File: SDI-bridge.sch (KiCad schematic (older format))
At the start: 24 parts

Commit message: Add todos
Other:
- note added: "TODO: Add logotypes, use Antmicro and OSHW"
- note added: "TODO: Add partitioning to schematics and names for functional blocks"
- note added: "TODO: clarify pin naming - SDI and SDI with dash on top"
- note added: "TODO: make sure the components used there are 1%"
- note added: "TODO: multiple schematics are nice but maybe it would be good to place everything on a single sheet (say A2 format) Still we can downscale it to A4 for printing on paper."
- note added: "TODO: place resistor ladders on OUT signals"
- note added: "TODO: place testpads on sync signals"
- note added: "TODO: please name particular nets in the bus/harness"
- note added: "Would be good to have an on-board LED indicator for LOCKED\nLOCKED should also be exposed on b2b connector"
- note added: "how about using 2 B2B connectors ?\ntreat audio signals with lowest priority"
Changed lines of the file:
@@
 EESchema Schematic File Version 4
 LIBS:SDI-bridge-cache
-EELAYER 26 0
+EELAYER 30 0
 EELAYER END
 $Descr A3 16535 11693
@@
 Wire Bus Line
 	3650 6850 3650 7750
+Text Notes 12250 6550 0    50   ~ 0
+TODO: make sure the components used there are 1%
+Text Notes 5950 4050 0    50   ~ 0
+TODO: clarify pin naming - SDI and SDI with dash on top
+Text Notes 4900 4050 1    50   ~ 0
+TODO: please name particular nets in the bus/harness
+Text Notes 1300 1550 0    50   ~ 0
+Would be good to have an on-board LED indicator for LOCKED\nLOCKED should also be exposed on b2b connector
+Text Notes 850  2050 0    50   ~ 0
+TODO: place testpads on sync signals
+Text Notes 4200 1750 0    50   ~ 0
+TODO: place resistor ladders on OUT signals
+Text Notes 1600 9050 0    50   ~ 0
+how about using 2 B2B connectors ?\ntreat audio signals with lowest priority
+Text Notes 2000 10050 0    50   ~ 0
+TODO: Add partitioning to schematics and names for functional blocks
+Text Notes 3000 11050 0    50   ~ 0
+TODO: multiple schematics are nice but maybe it would be good to place everything on a single sheet (say A2 format) Still we can downscale it to A4 for printing on paper.
+Text Notes 3050 10800 0    50   ~ 0
+TODO: Add logotypes, use Antmicro and OSHW
 $EndSCHEMATC

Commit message: Add updated schematic
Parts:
- added C1, C10, C11, C12, C13, C14, C19, C2, C20, C3, C31, C32, C4, C5, C6, C7, C8, C9, C?: C_10n_0402, antmicro-footprints:0402-cap, symbol antmicroCapacitors0402:C_10n_0402
- added C16: C_33u_0603, antmicro-footprints:0603, symbol antmicroCapacitorspol:C_33u_0603
- added C26, C27, C29, C30, C?: C_1u_0402, antmicro-footprints:0402-cap, symbol antmicroCapacitors0402:C_1u_0402
- added C? (x2): C_10u_0603, antmicro-footprints:0603-cap, symbol antmicroCapacitors0603:C_10u_0603
- added D?: LG_L29K-G2J1-24-Z, antmicro-footprints:LED_0603, symbol antmicroLEDIndicationDiscrete:LG_L29K-G2J1-24-Z
- added J?: 3220-10-0100-00, antmicro-footprints:PinHeader_2x5_P1.27mm_Drill.7mm, symbol antmicroRectangularConnectorsHeadersMalePins:3220-10-0100-00
- added R10, R11, R12, R13, R14, R15, R16, R17, R18, R19, R20, R21, R22, R23, R30, R31, R32, R4, R5, R6, R7, R8, R9: R_0R_0402, antmicro-footprints:0402-res, symbol antmicroResistors0402:R_0R_0402
- added R26: R_105R_0402, antmicro-footprints:0402-res, symbol antmicroResistors0402:R_105R_0402
- added R? (x2): R_120k_0402, antmicro-footprints:0402-res, symbol antmicroResistors0402:R_120k_0402
- added R?: R_100R_0402, antmicro-footprints:0402-res, symbol antmicroResistors0402:R_100R_0402
- added TP1, TP2, TP?: TP_SMD1MM, antmicro-footprints:Testpoint_smd_1mm, symbol antmicroTestPoints:TP_SMD1MM
- added U?: MAX8902B, antmicro-footprints:TDFN2x2, symbol antmicroPMICVoltageRegulatorsLinear:MAX8902B
- gave numbers to parts that had none: 22
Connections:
- net labels added: +3.3V, D0, D1, D10, D11, D12, D13, D14, D15, D16, D17, D18, D19, D2, D3, D4, D5, D6, D7, D8, D9, DOUT0, DOUT1, DOUT10, DOUT11, DOUT12, DOUT13, DOUT14, DOUT15, DOUT16, DOUT17, DOUT18, DOUT19, DOUT2, DOUT3, DOUT4, DOUT5, DOUT6, DOUT7, DOUT8, DOUT9, NC
- wire segments 206 -> 424
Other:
- note added: "Jtag"
- note added: "Power Filtering"
- note added: "Power decoupling"
- note removed: "TODO: Add logotypes, use Antmicro and OSHW"
- note removed: "TODO: make sure the components used there are 1%"
- note removed: "TODO: multiple schematics are nice but maybe it would be good to place everything on a single sheet (say A2 format) Still we can downscale it to A4 for printing on paper."
- note removed: "TODO: place resistor ladders on OUT signals"
- note removed: "TODO: place testpads on sync signals"
- note removed: "TODO: please name particular nets in the bus/harness"
- note removed: "Would be good to have an on-board LED indicator for LOCKED\nLOCKED should also be exposed on b2b connector"
- moved on the sheet: C15, C17, C18, C21, C22, C23, C24, C25, C28, J1, J2, R1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

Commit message: Arrange pcb components and add jumpers and logo
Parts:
- added JP1, JP2, JP3, JP4, JP5, JP6: SolderJumper_3_Open, Jumper:SolderJumper-3_P1.3mm_Open_Pad1.0x1.5mm, symbol Jumper:SolderJumper_3_Open
- added N1: antmicro_logo, antmicro-footprints:antmicro-logo_scaled_20mm, symbol antmicroMechanicalParts:antmicro_logo
- added R36, R37, R38, R39, R40, R41: R_0R_0402, antmicro-footprints:0402-res, symbol antmicroResistors0402:R_0R_0402
- gave numbers to parts that had none: 11
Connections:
- wire segments 424 -> 448
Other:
- note added: "Do we need SDO?"
- note added: "Low noise LDO\n"
- note added: "Power supply"
- note added: "Where to connect this signal?"
- note added: "treat audio signals with lowest priority"
- note removed: "Jtag"
- note removed: "We need to choose some of this signals( if needed more space we can change connector to bigger one)"
- note removed: "how about using 2 B2B connectors ?\ntreat audio signals with lowest priority"
- moved on the sheet: C1, C10, C11, C12, C13, C14, C15, C16, C17, C18, C19, C2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

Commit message: Initial routing -WIP
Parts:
- C16: footprint antmicro-footprints:0603 -> antmicro-footprints:0603-cap
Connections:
- net D0: now also R23.2; no longer R4.1
- net D1: now also R22.2; no longer R5.1
- net D10: now also R4.2; no longer R14.1
- net D11: now also R5.2; no longer R15.1
- net D12: now also R6.2; no longer R16.1
- net D13: now also R7.2; no longer R17.1
- net D14: now also R8.2; no longer R18.1
- net D15: now also R9.2; no longer R19.1
- net D16: now also R10.2; no longer R20.1
- net D17: now also R11.2; no longer R21.1
- net D18: now also R12.2; no longer R22.1
- net D19: now also R13.2; no longer R23.1
- net D2: now also R21.2; no longer R6.1
- net D3: now also R20.2; no longer R7.1
- net D4: now also R19.2; no longer R8.1
- net D5: now also R18.2; no longer R9.1
- net D6: now also R17.2; no longer R10.1
- net D7: now also R16.2; no longer R11.1
- net D8: now also R15.2; no longer R12.1
- net D9: now also R14.2; no longer R13.1
- net DOUT0: now also J1.40, R23.1; no longer J1.21, R4.2
- net DOUT1: now also J1.39, R22.1; no longer J1.22, R5.2
- net DOUT10: now also J1.30, R4.1; no longer J1.31, R14.2
- net DOUT11: now also J1.29, R5.1; no longer J1.32, R15.2
- net DOUT12: now also J1.28, R6.1; no longer J1.33, R16.2
- net DOUT13: now also J1.27, R7.1; no longer J1.34, R17.2
- net DOUT14: now also J1.26, R8.1; no longer J1.35, R18.2
- net DOUT15: now also J1.25, R9.1; no longer J1.36, R19.2
- net DOUT16: now also J1.24, R10.1; no longer J1.37, R20.2
- net DOUT17: now also J1.23, R11.1; no longer J1.38, R21.2
- net DOUT18: now also J1.22, R12.1; no longer J1.39, R22.2
- net DOUT19: now also J1.21, R13.1; no longer J1.40, R23.2
- net DOUT2: now also J1.38, R21.1; no longer J1.23, R6.2
- net DOUT3: now also J1.37, R20.1; no longer J1.24, R7.2
- net DOUT4: now also J1.36, R19.1; no longer J1.25, R8.2
- net DOUT5: now also J1.35, R18.1; no longer J1.26, R9.2
- net DOUT6: now also J1.34, R17.1; no longer J1.27, R10.2
- net DOUT7: now also J1.33, R16.1; no longer J1.28, R11.2
- net DOUT8: now also J1.32, R15.1; no longer J1.29, R12.2
- net DOUT9: now also J1.31, R14.1; no longer J1.30, R13.2
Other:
- moved on the sheet: R10, R11, R12, R13, R14, R15, R16, R17, R18, R19, R20, R21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

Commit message: Add routing - WIP
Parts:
- added R42: R_0R_0402, antmicro-footprints:0402-res, symbol antmicroResistors0402:R_0R_0402
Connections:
- net +3V3: now also R42.1; no longer C2.1, C33.1, C4.1, C6.1, C8.1, U1.A7 (IO_VDD), U1.D10 (IO_VDD), U1.G10 (IO_VDD), U1.K7 (IO_VDD)
- net GNDREF: now also C36.2
- new net +VSW: C2.1, C33.1, C4.1, C6.1, C8.1, R42.2, U1.A7 (IO_VDD), U1.D10 (IO_VDD), U1.G10 (IO_VDD), U1.K7 (IO_VDD)
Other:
- moved on the sheet: C36
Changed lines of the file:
@@
-$EndComp
-$Comp
-L antmicroCapacitors0603:C_10u_0603 C36
-U 1 1 5E2677C8
-P 10700 13000
-F 0 "C36" H 10815 13045 60  0000 L CNN
-F 1 "C_10u_0603" H 10700 12850 60  0001 C CNN
-F 2 "antmicro-footprints:0603-cap" H 10900 13200 60  0001 L CNN
-F 3 "" H 10700 13000 50  0001 C CNN
-F 4 "AVX" H 10900 13400 60  0001 L CNN "Manufacturer"
-F 5 "06036D106MAT2A" H 10900 13300 60  0001 L CNN "MPN"
-F 6 "10u" H 10815 12947 50  0000 L CNN "Val"
-	1    10700 13000
-	1    0    0    -1
 $EndComp
 $Comp
@@
 Connection ~ 10250 12850
 Wire Wire Line
-	10250 12850 10700 12850
-Wire Wire Line
-	10700 12850 11050 12850
-Connection ~ 10700 12850
-Wire Wire Line
 	9500 13200 10250 13200
 Wire Wire Line
@@
 $EndComp
 Wire Wire Line
-	13500 14850 13000 14850
+	13500 14850 13400 14850
 $Comp
 L antmicroCapacitors0402:C_1u_0402 C?
@@
 	-1   0    0    -1
 $EndComp
+$Comp
+L antmicroResistors0402:R_0R_0402 R?
+U 1 1 5E310B02
+P 13250 14850
+AR Path="/5DD55102/5E310B02" Ref="R?"  Part="1"
+AR Path="/5E310B02" Ref="R42"  Part="1"
+F 0 "R42" H 13250 15063 60  0000 C CNN
+F 1 "R_0R_0402" H 13250 14700 60  0001 C CNN
+F 2 "antmicro-footprints:0402-res" H 13450 15050 60  0001 L CNN
+F 3 "" H 13250 14850 50  0001 C CNN
+F 4 "PANASONIC" H 13450 15250 60  0001 L CNN "Manufacturer"
+F 5 "ERJ2GE0R00X" H 13450 15150 60  0001 L CNN "MPN"
+F 6 "0R" H 13250 14965 50  0000 C CNN "Val"
+	1    13250 14850
+	1    0    0    -1
+$EndComp
+Wire Wire Line
+	13100 14850 13000 14850
+$Comp
+L power:GNDREF #PWR?
+U 1 1 5E34416D
+P 10700 13900
+AR Path="/5DD55102/5E34416D" Ref="#PWR?"  Part="1"
+AR Path="/5E34416D" Ref="#PWR?"  Part="1"
+F 0 "#PWR?" H 10700 13650 50  0001 C CNN
+F 1 "GNDREF" H 10705 13727 50  0000 C CNN
+F 2 "" H 10700 13900 50  0001 C CNN
+F 3 "" H 10700 13900 50  0001 C CNN
+	1    10700 13900
+	1    0    0    -1
+$EndComp
+Wire Wire Line
+	10700 13250 10700 13900
+$Comp
+L antmicroCapacitors0603:C_10u_0603 C36
+U 1 1 5E2677C8
+P 10700 13100
+F 0 "C36" H 10815 13145 60  0000 L CNN
+F 1 "C_10u_0603" H 10700 12950 60  0001 C CNN
+F 2 "antmicro-footprints:0603-cap" H 10900 13300 60  0001 L CNN
+F 3 "" H 10700 13100 50  0001 C CNN
+F 4 "AVX" H 10900 13500 60  0001 L CNN "Manufacturer"
+F 5 "06036D106MAT2A" H 10900 13400 60  0001 L CNN "MPN"
+F 6 "10u" H 10815 13047 50  0000 L CNN "Val"
+	1    10700 13100
+	1    0    0    -1
+$EndComp
+Wire Wire Line
+	10250 12850 10700 12850
+Wire Wire Line
+	10700 12950 10700 12850
 Wire Bus Line
 	4750 1850 4750 2750
@@
 Wire Bus Line
 	4750 2850 4750 3750
+Connection ~ 10700 12850
+Wire Wire Line
+	10700 12850 11050 12850
 $EndSCHEMATC

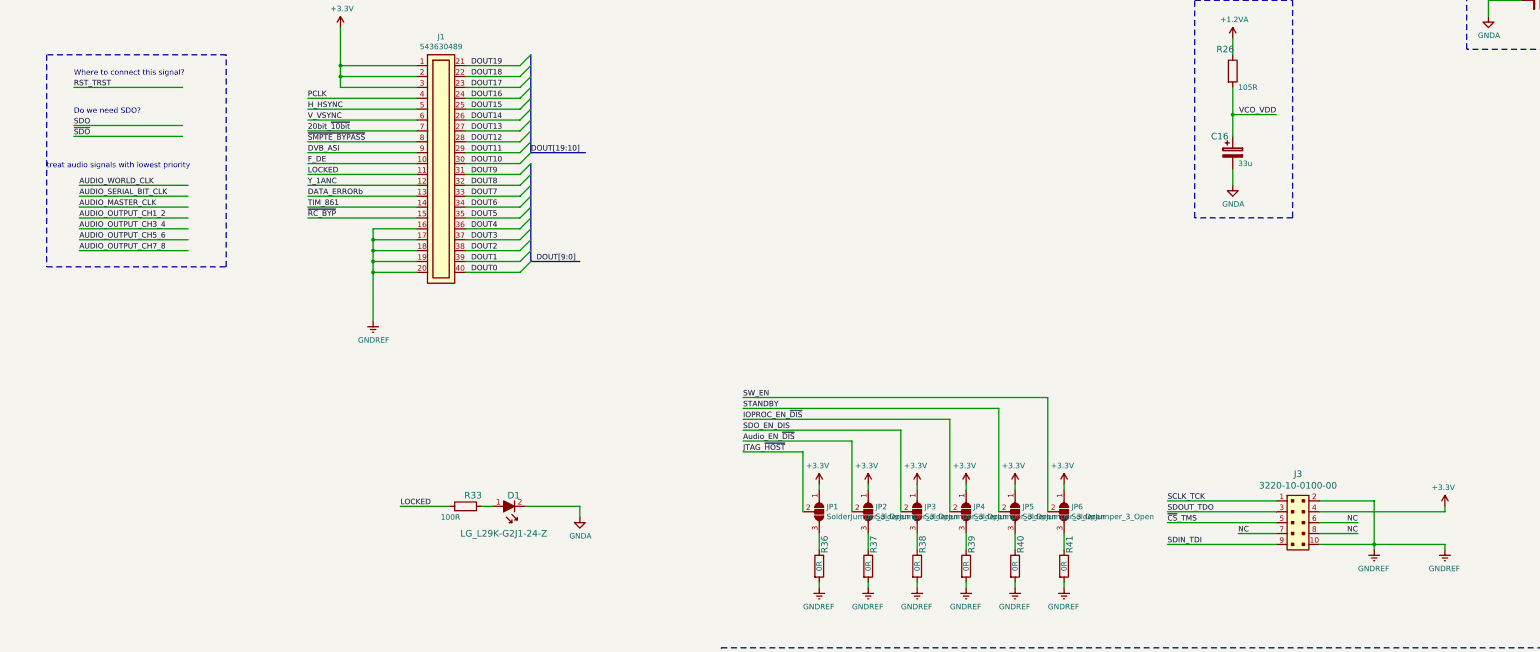
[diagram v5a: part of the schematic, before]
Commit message: Add complete routing
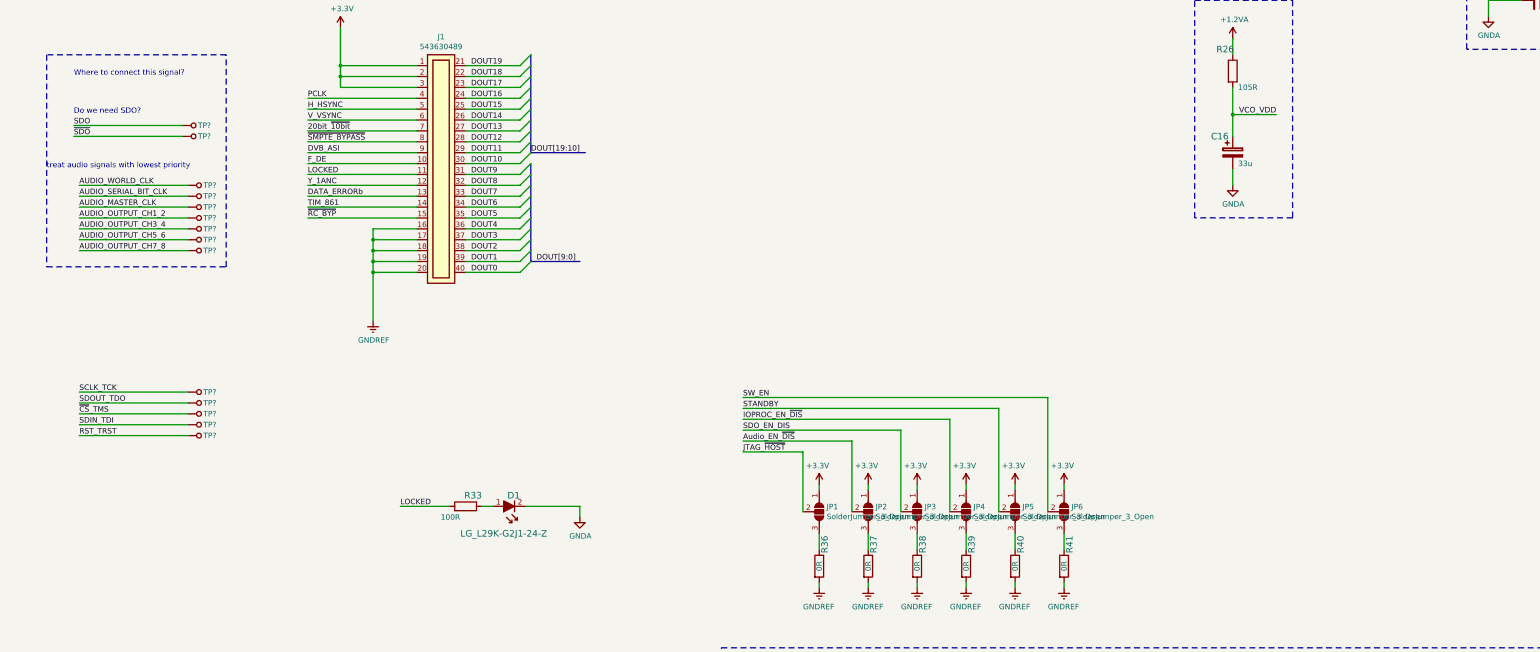
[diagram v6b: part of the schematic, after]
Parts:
- removed J3: 3220-10-0100-00, antmicro-footprints:PinHeader_2x5_P1.27mm_Drill.7mm, symbol antmicroRectangularConnectorsHeadersMalePins:3220-10-0100-00
- added TP? (x14): TP_SMD1MM, antmicro-footprints:Testpoint_smd_1mm, symbol antmicroTestPoints:TP_SMD1MM
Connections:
- net AUDIO_MASTER_CLK: now also TP?.1
- net AUDIO_OUTPUT_CH1_2: now also TP?.1
- net AUDIO_OUTPUT_CH3_4: now also TP?.1
- net AUDIO_OUTPUT_CH5_6: now also TP?.1
- net AUDIO_OUTPUT_CH7_8: now also TP?.1
- net AUDIO_SERIAL_BIT_CLK: now also TP?.1
- net AUDIO_WORLD_CLK: now also TP?.1
- net RST_TRST: now also TP?.1
- net SCLK_TCK: now also TP?.1
- net SDIN_TDI: now also TP?.1
- net SDO: now also TP?.1
- net SDOUT_TDO: now also TP?.1
- net ~CS~_TMS: now also TP?.1
- net ~SDO~: now also TP?.1

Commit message: Schematic cleanup
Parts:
- removed TP? (x2): TP_SMD1MM, antmicro-footprints:Testpoint_smd_1mm, symbol antmicroTestPoints:TP_SMD1MM
- added J1: 22-23-2021, antmicro-footprints:PinHeader_1x2_P2.54mm_Drill1.02mm, symbol antmicroRectangularConnectorsHeadersMalePins:22-23-2021
- gave numbers to parts that had none: 12
- renumbered C34 to C1, C29 to C10, C30 to C11, C31 to C12, C32 to C13, C21 to C14, C22 to C15, C23 to C16, C24 to C17, C25 to C18, C28 to C19, C35 to C2, C1 to C20, C2 to C21, C3 to C22, C4 to C23, C5 to C24, C6 to C25, C7 to C26, C8 to C27, C9 to C28, C10 to C29, C36 to C3, C11 to C30, C12 to C31, C13 to C32, C14 to C33, C15 to C34, C17 to C35, C18 to C36, C16 to C4, C19 to C5, C20 to C6, C26 to C7, C27 to C8, C33 to C9, J1 to J2, J2 to J3, R17 to R10, R16 to R11, R15 to R12, R14 to R13, R4 to R14, R5 to R15, R6 to R16, R7 to R17, R8 to R18, R9 to R19, R10 to R20, R11 to R21, R12 to R22, R13 to R23, R33 to R24, R36 to R25, R37 to R26, R38 to R27, R39 to R28, R40 to R29, R41 to R30, R34 to R31, R35 to R32, R26 to R33, R42 to R34, R30 to R35, R31 to R36, R32 to R37, R28 to R38, R29 to R39, R23 to R4, R24 to R40, R25 to R41, R27 to R42, R22 to R5, R21 to R6, R20 to R7, R19 to R8, R18 to R9, TP3 to TP15, TP4 to TP16
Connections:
- net SDO: now also J1.2
- net ~SDO~: now also J1.1
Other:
- note added: "Audio signals"
- note added: "Configurable pins"
- note added: "Filtering"
- note added: "JTAG Signals"
- note added: "Locked_signal_led"
- note added: "Logo"
- note added: "SDO\n"
- note added: "clock"
- note removed: "Do we need SDO?"
- note removed: "TODO: Add partitioning to schematics and names for functional blocks"
- note removed: "TODO: clarify pin naming - SDI and SDI with dash on top"
- note removed: "Where to connect this signal?"
- note removed: "treat audio signals with lowest priority"
- moved on the sheet: C1, C10, C11, C12, C13, C2, C20, C21, C22, C23, C24, C25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

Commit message: Add CrossLink to schematic
Also changed:
-add 50-pin mipi connector
-remove b2b connector
-remove jumpers and conect signals to fpga
-remove audio testpats and connect signals to fpga
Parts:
- removed J1: 22-23-2021, antmicro-footprints:PinHeader_1x2_P2.54mm_Drill1.02mm, symbol antmicroRectangularConnectorsHeadersMalePins:22-23-2021
- removed J2: 543630489, antmicro-footprints:543630489, symbol antmicroB2bConnectors:543630489
- removed JP1, JP2, JP3, JP4, JP5, JP6: SolderJumper_3_Open, Jumper:SolderJumper-3_P1.3mm_Open_Pad1.0x1.5mm, symbol Jumper:SolderJumper_3_Open
- removed R25, R26, R27, R28, R29, R30: R_0R_0402, antmicro-footprints:0402-res, symbol antmicroResistors0402:R_0R_0402
- removed TP10, TP11, TP12, TP13, TP14, TP3, TP4, TP5, TP6, TP7, TP8, TP9: TP_SMD1MM, antmicro-footprints:Testpoint_smd_1mm, symbol antmicroTestPoints:TP_SMD1MM
- added C?: C_5n6_0402, antmicro-footprints:0402-res, symbol antmicroCapacitors0402:C_5n6_0402
- added C? (x5): C_10n_0402, antmicro-footprints:0402-cap, symbol antmicroCapacitors0402:C_10n_0402
- added C? (x2): C_1u_0402, antmicro-footprints:0402-cap, symbol antmicroCapacitors0402:C_1u_0402
- added C? (x2): C_4u7_0402, antmicro-footprints:0402-cap, symbol antmicroCapacitors0402:C_4u7_0402
- added J?: 031-70526-21, antmicro-footprints:BNC_Edge_Conn, symbol antmicroCoaxialConnectorsRF:031-70526-21
- added J?: WE_68715014522, antmicro-footprints:WE_68715014522, symbol antmicroFCCConnectors:WE_68715014522
- added R?: R_750R_0402, antmicro-footprints:0402-res, symbol antmicroResistors0402:R_750R_0402
- added R? (x2): R_0R_0402, antmicro-footprints:0402-res, symbol antmicroResistors0402:R_0R_0402
- added R? (x4): R_75R_0603, antmicro-footprints:0603-res, symbol antmicroResistors0603:R_75R_0603
- added R? (x4): R_2k37_0402, antmicro-footprints:0402-res, symbol antmicroResistors0402:R_2k37_0402
- added U?: CrossLink_LIF-MD6000-6JMG80I, symbol antmicroBGAchips:CrossLink_LIF-MD6000-6JMG80I
- added U?: GS2988, symbol antmicroInterfaceControllers:GS2988
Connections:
- net labels added: AUDIO_WORD_CLK, CAM_RST, M1_CAM_SCL, M1_CAM_SDA, M2_CAM_SCL, M2_CAM_SDA, MIPI_CLK_N, MIPI_CLK_P, MIPI_D0_N, MIPI_D0_P, MIPI_D1_N, MIPI_D1_P, MIPI_D2_N, MIPI_D2_P, MIPI_D3_N, MIPI_D3_P, VDD
- net labels removed: AUDIO_WORLD_CLK
- wire segments 440 -> 505
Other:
- note added: "DNP"
- note added: "SPI"
- note removed: "Audio signals"
- note removed: "B2B Connector\n"
- note removed: "Configurable pins"
- note removed: "JTAG Signals"
- moved on the sheet: C10, C11, C12, C13, C5, C6, C7, C8, R35, R36, R37
